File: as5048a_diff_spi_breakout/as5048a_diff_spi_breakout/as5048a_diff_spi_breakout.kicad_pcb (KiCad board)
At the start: 2 copper layers, 48 x 28 mm, 12 parts, among them J1 Conn_01x02, J2 8P8C, U1 SN65LVDT14, U2 AS5048A

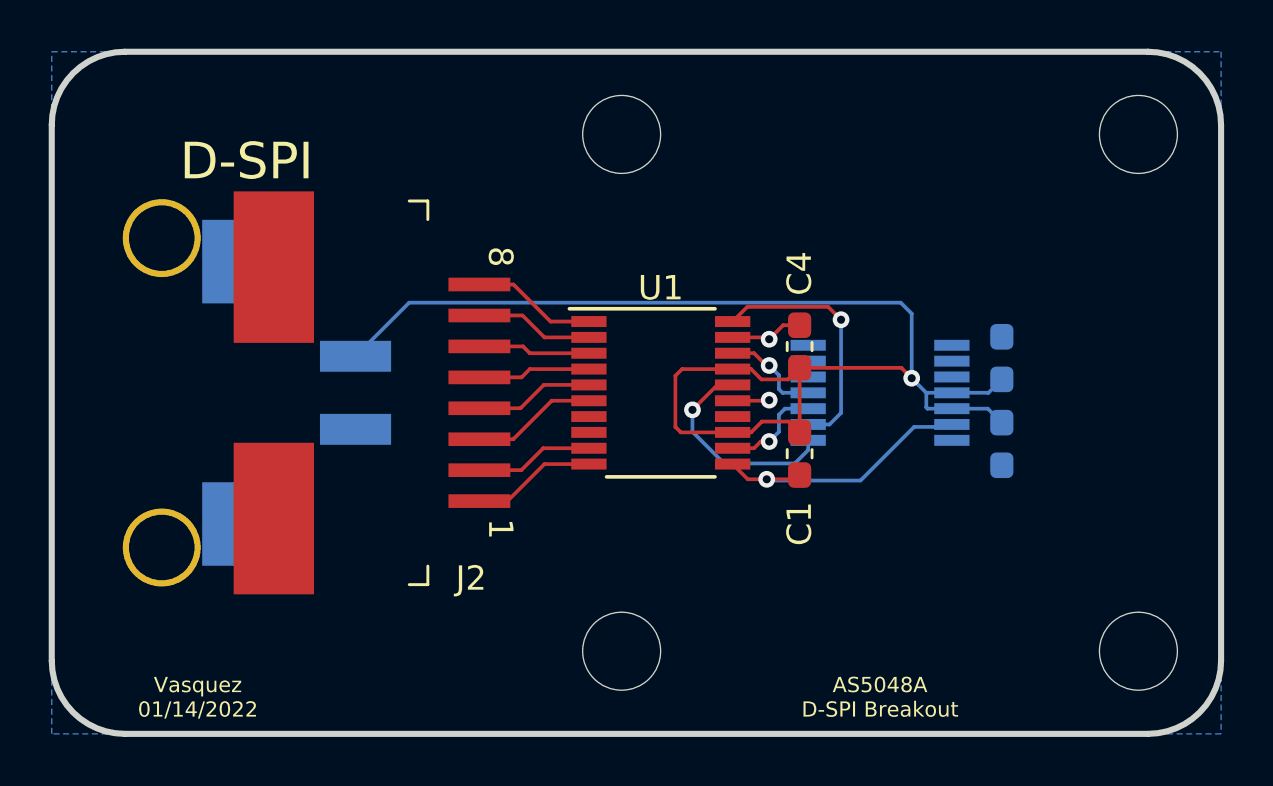
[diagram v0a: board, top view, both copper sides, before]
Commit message: adding pareto leg kins
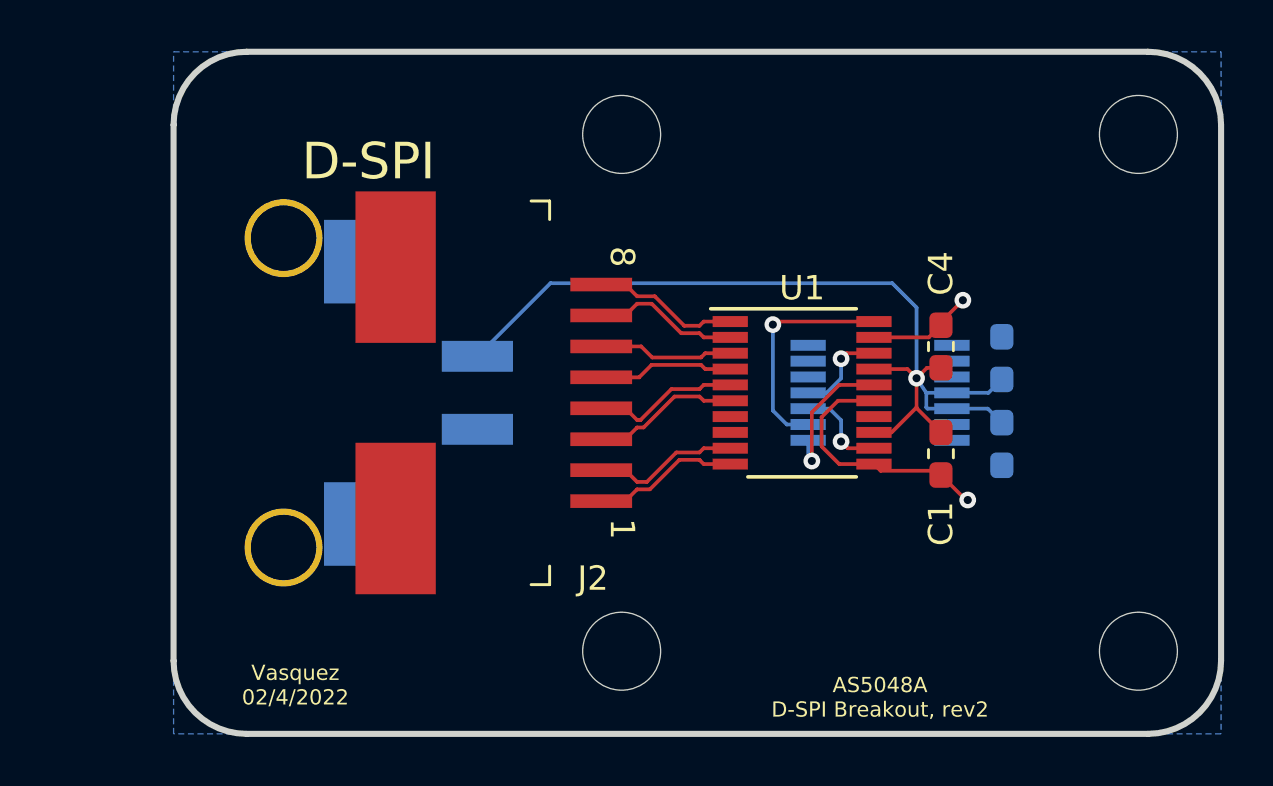
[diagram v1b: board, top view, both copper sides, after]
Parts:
- moved C1 5.80 mm to (138.5, 106.4)
- moved C4 5.80 mm to (138.5, 102.0)
- moved U1 5.80 mm to (132.8, 103.9)
- moved J1 5.00 mm to (114.0, 103.9)
- moved J2 5.00 mm to (115.0, 103.9)
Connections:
- net Net-(J2-Pad1) renamed /MISO_N
- net Net-(J2-Pad2) renamed /MISO_P
- net Net-(J2-Pad3) renamed /CS_N
- net Net-(J2-Pad4) renamed /CS_P
- net Net-(J2-Pad5) renamed /MOSI_N
- net Net-(J2-Pad6) renamed /MOSI_P
- net Net-(J2-Pad7) renamed /SCK_N
- net Net-(J2-Pad8) renamed /SCK_P
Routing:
- net +3V3: track 55.4 -> 38.5 mm
- net /CSx: track 8.89 -> 5.93 mm
- net GND: track 16.2 -> 14.9 mm, vias 3 -> 2
- net /CS_P: track 4.89 -> 6.09 mm
- net /MISO_P: track 4.87 -> 6.07 mm
- net /SCK_N: track 4.87 -> 6.07 mm
- net /MOSI_P: track 4.61 -> 5.56 mm
- net /CS_N: track 5.15 -> 6.09 mm
- net /MISO_N: track 5.12 -> 6.07 mm
- net /SCK_P: track 5.12 -> 6.07 mm
- net /MOSI_N: track 4.64 -> 5.58 mm
- net /SCK: track 10.3 -> 9.42 mm
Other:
- board size 48 x 28 mm -> 43 x 28 mm
- board text added: "AS5048A D-SPI Breakout, rev2"
- board text added: "Vasquez 02/4/2022"
- board text removed: "AS5048A D-SPI Breakout"
- board text removed: "Vasquez 01/14/2022"
